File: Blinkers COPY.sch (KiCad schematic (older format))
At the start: 219 parts, among them J1 12V, J2 A1, J3 gnd, J4 A1, J5 A1, J6 A1, J7 A1, J8 A1, J9 brake, Q1 Q_NMOS_DGS, Q2 Q_NMOS_DGS, Q3 Q_NMOS_DGS, Q4 Q_NMOS_DGS, Q5 Q_NMOS_DGS, Q6 Q_NMOS_DGS

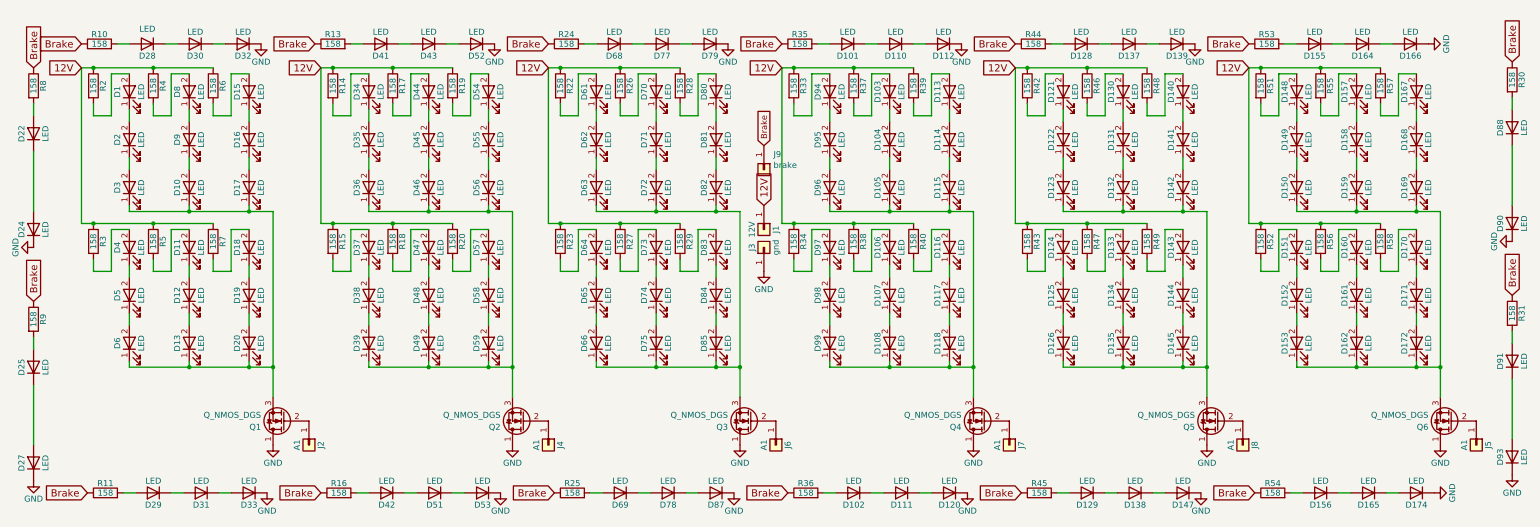
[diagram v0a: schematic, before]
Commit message: Nova_Layout_1-1
Fixed LED footprint, small pad is GND, large pad is positive. This is opposite of the data sheet.

Adjusted position of some components for better fit (and fixed R48 and R49)

Switched the input pins for the transistors to fit a 3x1 set of pins with 2.54mm pitch.

Changed inner resistor and outer resistor footprints to match original outer footprints.

Checked all reference numbers to make sure they were the correct size and will be readable when soldering.
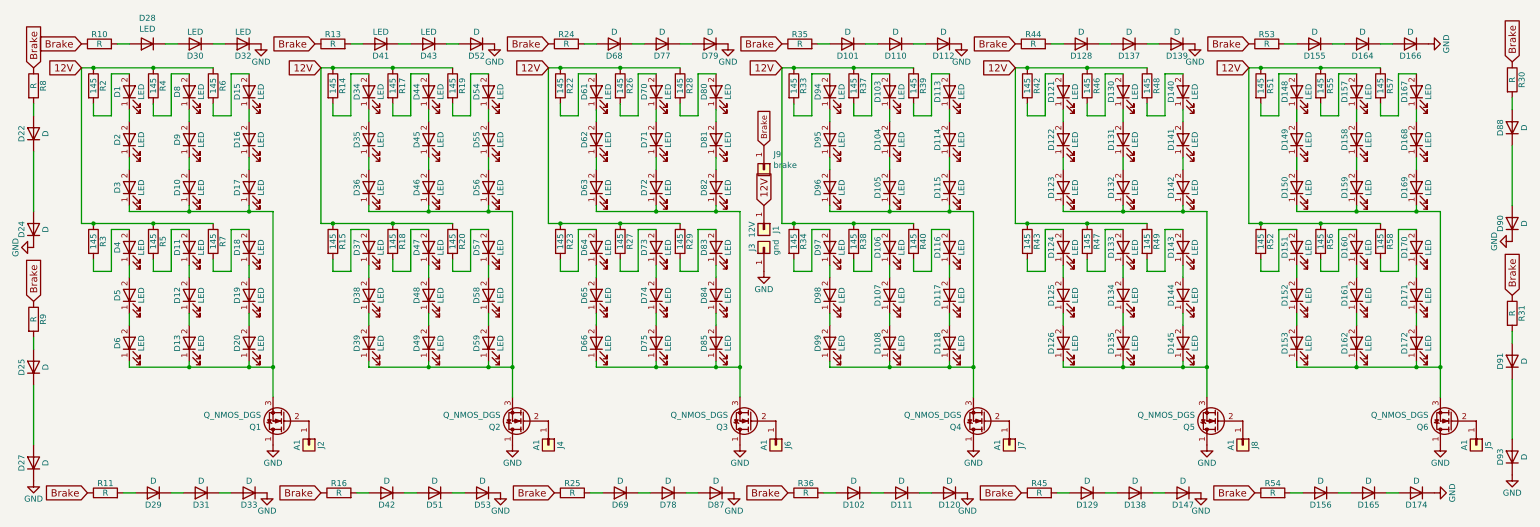
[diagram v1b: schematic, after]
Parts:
- D101, D102, D110, D111, D112, D120, D128, D129, D137, D138, D139, D147, D155, D156, D164, D165, D166, D174, D22, D24, D25, D27, D29, D31, D33, D42, D51, D52, D53, D68, D69, D77, D78, D79, D87, D88, D90, D91, D93: value LED -> D
- J2: footprint Socket_Strips:Socket_Strip_Straight_1x01_Pitch2.54mm -> Socket_Strips:Socket_Strip_Straight_1x03_Pitch2.54mm
- R10, R11, R13, R16, R24, R25, R30, R31, R35, R36, R44, R45, R53, R54, R8, R9: value 158 -> R; footprint Resistor_SMD:R_1210_3225Metric -> Resistors_SMD:R_1206
- R14, R15, R17, R18, R19, R2, R20, R22, R23, R26, R27, R28, R29, R3, R33, R34, R37, R38, R39, R4, R40, R42, R43, R46, R47, R48, R49, R5, R51, R52, R55, R56, R57, R58, R6, R7: value 158 -> 145; footprint Resistor_SMD:R_1210_3225Metric -> Resistors_SMD:R_1206
